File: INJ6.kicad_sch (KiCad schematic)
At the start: 9 parts, among them U7 VNLD5160TR-E, U8 VNLD5160TR-E, U9 VNLD5160TR-E

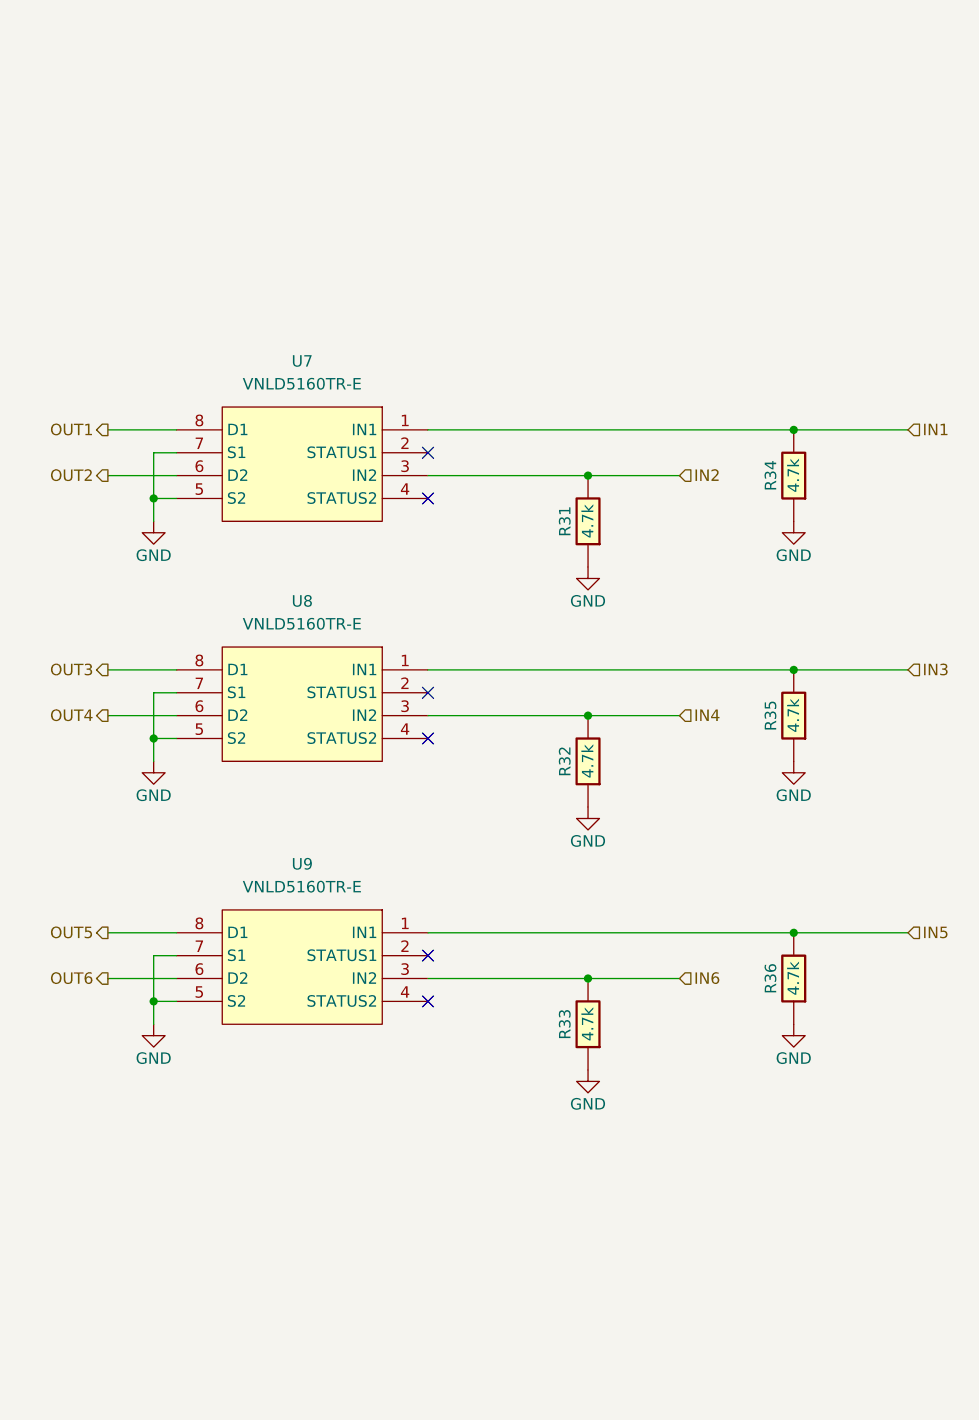
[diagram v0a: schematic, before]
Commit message: colocacion de los componentes en un 90%
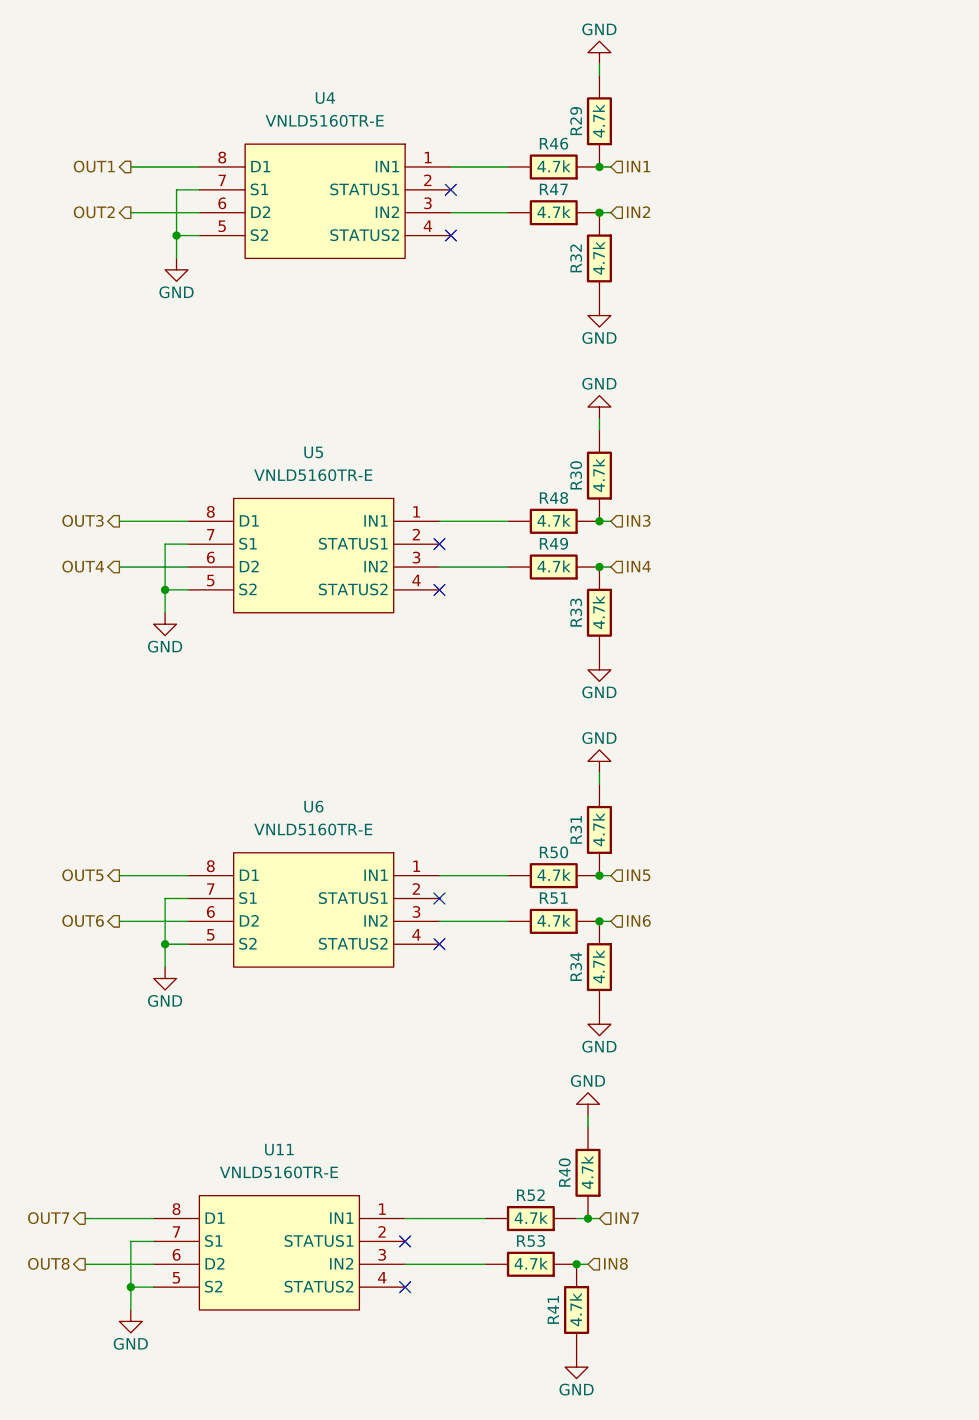
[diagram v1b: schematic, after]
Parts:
- removed R35, R36: 4.7k, hellen-one-common:R0603, symbol hellen-one-common:Res
- added R29, R30, R40, R41, R46, R47, R48, R49, R50, R51, R52, R53: 4.7k, hellen-one-common:R0603, symbol hellen-one-common:Res
- added U11: VNLD5160TR-E, Package_SO:SOIC-8_3.9x4.9mm_P1.27mm, symbol chips:VNLD5160
- renumbered U7 to U4, U8 to U5, U9 to U6
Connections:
- net GND: now also R31.2, R32.2, R33.2, R34.2, R29.2, R30.2, R40.2, R41.2, U11.5 (S2), U11.7 (S1); no longer R31.1, R32.1, R33.1, R34.1
- net IN1: now also R29.1, R46.1; no longer R34.2, U4.1 (IN1)
- net IN2: now also R32.1, R47.1; no longer R31.2, U4.3 (IN2)
- net IN3: now also R30.1, R48.1; no longer U5.1 (IN1)
- net IN4: now also R33.1, R49.1; no longer R32.2, U5.3 (IN2)
- net IN5: now also R31.1, R50.1; no longer U6.1 (IN1)
- net IN6: now also R34.1, R51.1; no longer R33.2, U6.3 (IN2)
- new net: R51.2, U6.3 (IN2)
- new net: R49.2, U5.3 (IN2)
- new net: R50.2, U6.1 (IN1)
- new net: R53.2, U11.3 (IN2)
- new net: R47.2, U4.3 (IN2)
- new net: R46.2, U4.1 (IN1)
- new net: R48.2, U5.1 (IN1)
- new net: R52.2, U11.1 (IN1)
- new net IN7: R40.1, R52.1
- new net IN8: R41.1, R53.1
- new net OUT7: U11.8 (D1)
- new net OUT8: U11.6 (D2)
- no-connect marks 6 -> 8
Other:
- moved on the sheet: U4, U5, U6
